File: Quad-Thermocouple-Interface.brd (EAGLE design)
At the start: 57.1 x 50.8 mm, 21 parts

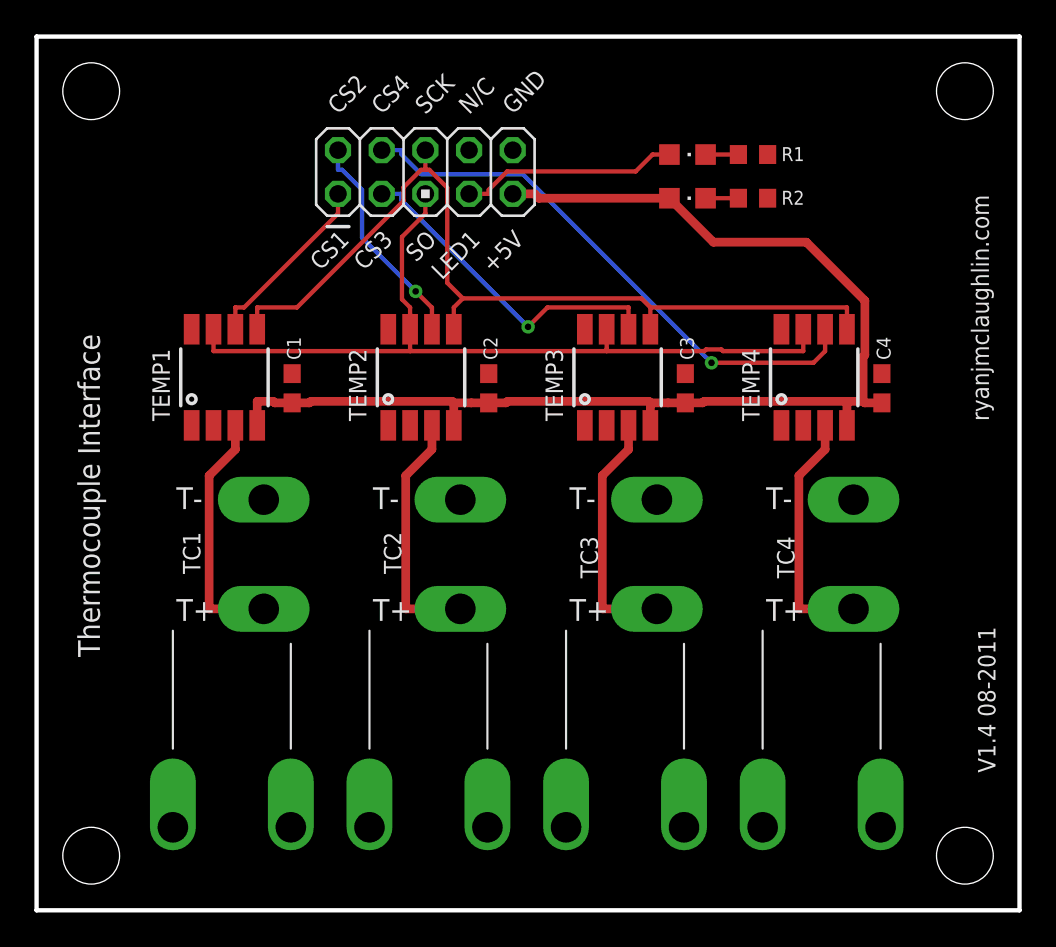
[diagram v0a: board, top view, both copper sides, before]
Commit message: Updated with level shifter and power supply for MAX31855, rev to v2.0
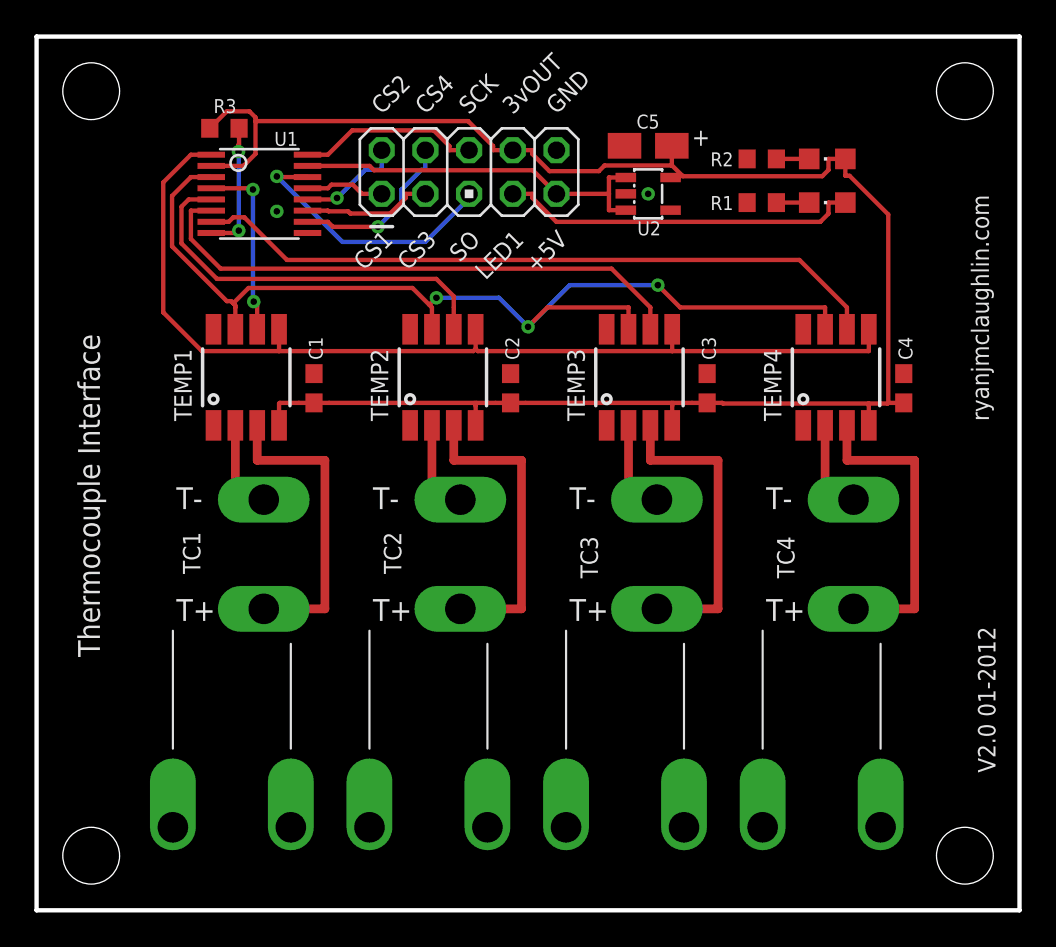
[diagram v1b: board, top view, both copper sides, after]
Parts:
- added C5: 10uF/10V, adafruit:A/3216-18R
- added R3: 10K, resistor:R0603
- added U1: TXB0106PWR, McLEng:TSSOP16
- added U2: LP298XS, adafruit:SOT23-5L
- TEMP1, TEMP2, TEMP3, TEMP4: value MAX6675MAX6675 -> MAX31855
- moved LED1 8.59 mm to (46.0, 41.1), turned to 90 degrees
- moved LED2 8.44 mm to (46.0, 43.7), turned to 90 degrees
- moved R1 2.84 mm to (42.2, 41.1), turned to 180 degrees
- moved JP1 2.54 mm to (25.1, 42.9)
- moved R2 2.34 mm to (42.2, 43.7), turned to 180 degrees
- moved TEMP3 1.27 mm to (35.1, 31.0)
- moved C1 1.27 mm to (16.1, 30.4)
- moved C2 1.27 mm to (27.6, 30.4)
- moved TEMP1 1.27 mm to (12.2, 31.0)
- moved TEMP2 1.27 mm to (23.6, 31.0)
- moved C3 1.27 mm to (39.0, 30.4)
- moved C4 1.27 mm to (50.4, 30.4)
- moved TEMP4 1.27 mm to (46.5, 31.0)
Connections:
- net N$1 renamed LED1
- net N$12 renamed T4
- net N$3 renamed T1
- net N$6 renamed T2
- net N$9 renamed T3
- removed net VCC: C1.1, C2.1, C3.1, C4.1, JP1.9, LED2.A, TEMP1.VCC, TEMP2.VCC, TEMP3.VCC, TEMP4.VCC
- new net +3V3: C1.1, C2.1, C3.1, C4.1, C5.+, JP1.8, LED2.A, R3.1, TEMP1.VCC, TEMP2.VCC, TEMP3.VCC, TEMP4.VCC, U1.2, U2.5
- new net +5V: JP1.9, U1.15, U2.1, U2.3
- new net N$1: R3.2, U1.8
- new net T1-: TC1.T-, TEMP1.T-
- new net T2-: TC2.T-, TEMP2.T-
- new net T3-: TC3.T-, TEMP3.T-
- new net T4-: TC4.T-, TEMP4.T-
- new net _CS1: JP1.1, U1.13
- new net _CS2: JP1.2, U1.12
- new net _CS3: JP1.3, U1.11
- new net _CS4: JP1.4, U1.10
- new net _SCK: JP1.6, U1.16
- new net _SO: JP1.5, U1.14
- net CS1: now also U1.4; no longer JP1.1
- net CS2: now also U1.5; no longer JP1.2
- net CS3: now also U1.6; no longer JP1.3
- net CS4: now also U1.7; no longer JP1.4
- net GND: now also C5.-, U1.9, U2.2; no longer TC1.T-, TC2.T-, TC3.T-, TC4.T-, TEMP1.T-, TEMP2.T-, TEMP3.T-, TEMP4.T-
- net SCK: now also U1.1; no longer JP1.6
- net SO: now also U1.3; no longer JP1.5
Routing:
- net +3V3: track 0.00 -> 103.9 mm
- net VCC: track 70.9 -> 0.00 mm
- net +5V: track 0.00 -> 22.1 mm
- net _SO: track 0.00 -> 15.9 mm, vias 0 -> 1
- net CS3: track 19.5 -> 32.5 mm, vias 1 -> 0
- net SO: track 48.1 -> 60.1 mm, vias 0 -> 3
- net _SCK: track 0.00 -> 10.6 mm
- net CS2: track 12.8 -> 23.1 mm, vias 1 -> 0
- net _CS4: track 0.00 -> 9.95 mm, vias 0 -> 1
- net LED1: track 12.7 -> 21.0 mm
- net CS4: track 32.6 -> 40.5 mm, vias 1 -> 0
- net N$1: track 0.00 -> 7.63 mm, vias 0 -> 2
- net _CS3: track 0.00 -> 7.53 mm
- net SCK: track 51.6 -> 58.0 mm
- net _CS2: track 0.00 -> 6.17 mm, vias 0 -> 1
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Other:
- board text added: "3vOUT"
- board text added: "V2.0 01-2012"
- board text removed: "N/C"
- board text removed: "V1.4 08-2011"
